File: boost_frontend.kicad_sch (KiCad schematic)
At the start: 25 parts, among them Q1 Q_NMOS, U1 LT8342RV-TRMPBF

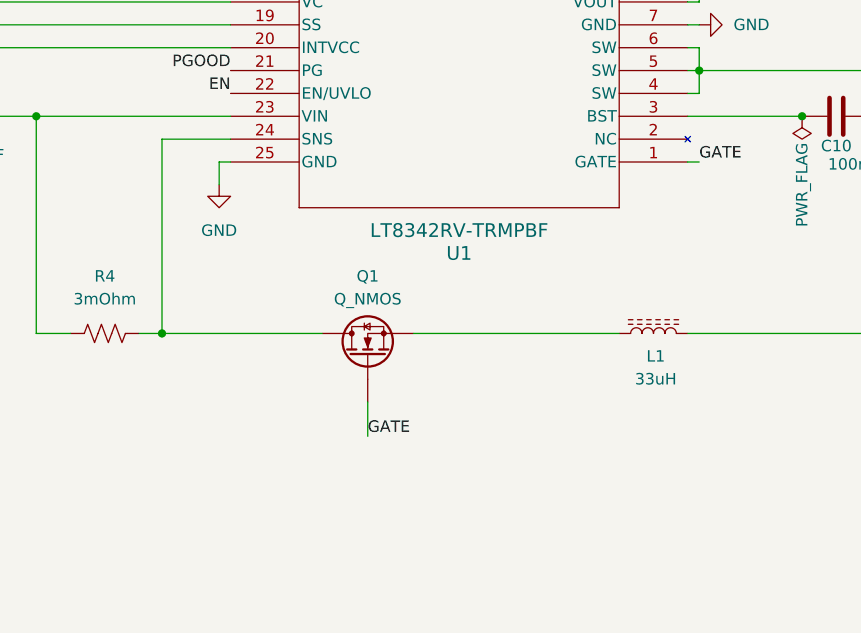
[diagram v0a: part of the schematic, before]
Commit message: routing for power completed
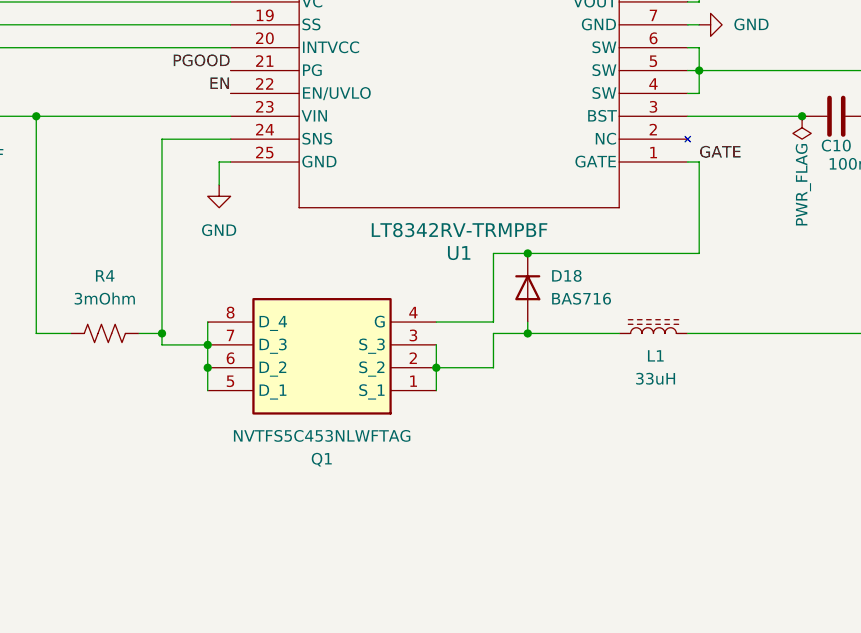
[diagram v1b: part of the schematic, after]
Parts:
- removed Q1: Q_NMOS, Package_DFN_QFN:WDFN-8-1EP_2x2.2mm_P0.5mm_EP0.80x0.54, symbol Device:Q_NMOS
- added D18: BAS716, Diode_SMD:D_SOD-523, symbol Device:D
- added Q1: NVTFS5C453NLWFTAG, NVTFS6H854NTAG, symbol _NVTF:NVTFS5C453NLWFTAG
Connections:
- net GATE: now also D18.1 (K), Q1.4 (G)
- net at R4.2, U1.24 (SNS): now also Q1.5 (D_1), Q1.6 (D_2), Q1.7 (D_3), Q1.8 (D_4)
- net at L1.1: now also D18.2 (A), Q1.1 (S_1), Q1.2 (S_2), Q1.3 (S_3)

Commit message: Working on it
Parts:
- C15, C16, FB2: now not fitted; now left out of the parts list
- renumbered D18 to D1
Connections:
- net Vout is gone; now on net BOOST_OUT: C11.1, C12.1, C13.2, C14.2, FB2.1, U1.10 (VOUT), U1.11 (VOUT), U1.8 (VOUT), U1.9 (VOUT)
- net GND: now also C5.2; no longer C5.1
- net INTVCC: now also R3.2; no longer R3.1
- net at U1.19 (SS): now also C5.1; no longer C5.2
- net at U1.14 (VSET1): now also R3.1; no longer R3.2
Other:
- moved on the sheet: C1, C10, C11, C12, C13, C14, C2, C3, C4, C5, C6, C7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

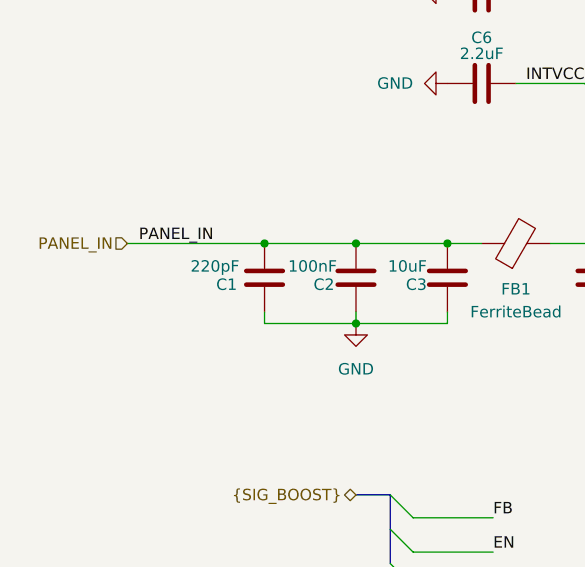
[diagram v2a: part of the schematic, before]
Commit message: Eiditng frontend
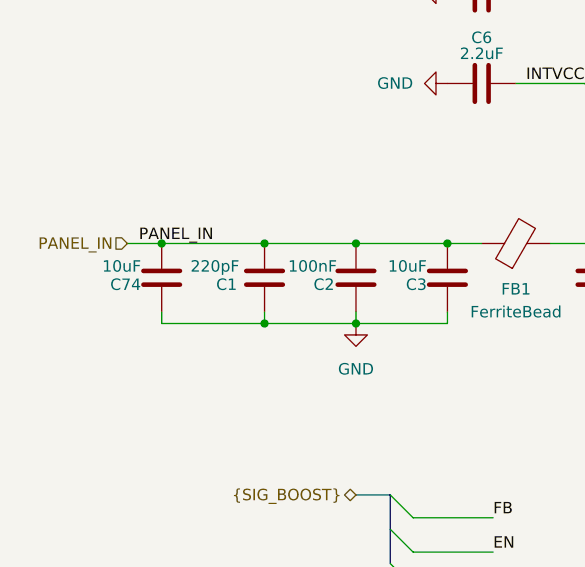
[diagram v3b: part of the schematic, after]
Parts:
- added C74: 10uF, Capacitor_SMD:C_0805_2012Metric, symbol Device:C
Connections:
- net GND: now also C74.1
- net PANEL_IN: now also C74.2
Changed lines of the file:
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@@
+	)
+	(junction
+		(at 31.75 104.14)
+		(diameter 0)
+		(color 0 0 0 0)
 	)
 	(junction
@@
 	(junction
 		(at 154.94 132.08)
+		(diameter 0)
+		(color 0 0 0 0)
+	)
+	(junction
+		(at 43.18 113.03)
 		(diameter 0)
 		(color 0 0 0 0)
@@
 	(wire
 		(pts
+			(xy 31.75 111.76) (xy 31.75 113.03)
+		)
+		(stroke
+			(width 0)
+			(type default)
+		)
+	)
+	(wire
+		(pts
 			(xy 53.34 113.03) (xy 63.5 113.03)
 		)
@@
 	(wire
 		(pts
+			(xy 31.75 113.03) (xy 43.18 113.03)
+		)
+		(stroke
+			(width 0)
+			(type default)
+		)
+	)
+	(wire
+		(pts
 			(xy 132.08 86.36) (xy 124.46 86.36)
 		)
@@
 	(wire
 		(pts
-			(xy 27.94 104.14) (xy 43.18 104.14)
+			(xy 27.94 104.14) (xy 31.75 104.14)
 		)
 		(stroke
@@
 		(pts
 			(xy 100.33 113.03) (xy 100.33 111.76)
+		)
+		(stroke
+			(width 0)
+			(type default)
+		)
+	)
+	(wire
+		(pts
+			(xy 31.75 104.14) (xy 43.18 104.14)
 		)
 		(stroke
@@
 					(unit 1)
 				)
+			)
+		)
+	)
+	(symbol
+		(lib_id "Device:C")
+		(at 31.75 107.95 180)
+		(unit 1)
+		(exclude_from_sim no)
+		(in_bom yes)
+		(on_board yes)
+		(dnp no)
+		(property "Reference" "C74"
+			(at 29.464 108.712 0)
+			(effects
+				(font
+					(size 1.27 1.27)
+				)
+				(justify left)
+			)
+		)
+		(property "Value" "10uF"
+			(at 29.464 106.68 0)
+			(effects
+				(font
+					(size 1.27 1.27)
+				)
+				(justify left)
+			)
+		)
+		(property "Footprint" "Capacitor_SMD:C_0805_2012Metric"
+			(at 30.7848 104.14 0)
+			(effects
+				(font
+					(size 1.27 1.27)
+				)
+				(hide yes)
+			)
+		)
+		(property "Datasheet" "https://search.murata.co.jp/Ceramy/image/img/A01X/G101/ENG/GRM21BR61H106KE43-01A.pdf"
+			(at 31.75 107.95 0)
+			(effects
+				(font
+					(size 1.27 1.27)
+				)
+				(hide yes)
+			)
+		)
+		(property "Description" "CAP CER 10UF 50V X5R 0805"
+			(at 31.75 107.95 0)
+			(effects
+				(font
+					(size 1.27 1.27)
+				)
+				(hide yes)
+			)
+		)
+		(property "Mfr" "Murata Electronics"
+			(at 31.75 107.95 0)
+			(effects
+				(font
+					(size 1.27 1.27)
+				)
+				(hide yes)
+			)
+		)
+		(property "Mfr P/N" "GRM21BR61H106KE43L"
+			(at 31.75 107.95 0)
+			(effects
+				(font
+					(size 1.27 1.27)
+				)
+				(hide yes)
+			)
+		)
+		(property "Supplier_1" "Digikey"
+			(at 31.75 107.95 0)
+			(effects
+				(font
+					(size 1.27 1.27)
+				)
+				(hide yes)
+			)
+		)
+		(property "Supplier_1 P/N" "490-18663-2-ND"
+			(at 31.75 107.95 0)
+			(effects
+				(font
+					(size 1.27 1.27)
+				)
+				(hide yes)
+			)
+		)
+		(property "Supplier_1 Unit Price" "0.28000"
+			(at 31.75 107.95 0)
+			(effects
+				(font
+					(size 1.27 1.27)
+				)
+				(hide yes)
+			)
+		)
+		(property "Supplier_1 Price @ Qty" "1"
+			(at 31.75 107.95 0)
+			(effects
+				(font
+					(size 1.27 1.27)
+				)
+				(hide yes)
+			)
+		)
+		(property "Supplier_2" ""
+			(at 31.75 107.95 0)
+			(effects
+				(font
+					(size 1.27 1.27)
+				)
+				(hide yes)
+			)
+		)
+		(property "Supplier_2 P/N" ""
+			(at 31.75 107.95 0)
+			(effects
+				(font
+					(size 1.27 1.27)
+				)
+				(hide yes)
+			)
+		)
+		(property "Supplier_2 Unit Price" ""
+			(at 31.75 107.95 0)
+			(effects
+				(font
+					(size 1.27 1.27)
+				)
+				(hide yes)
+			)
+		)
+		(property "Supplier_2 Price @ Qty" ""
+			(at 31.75 107.95 0)
+			(effects
+				(font
+					(size 1.27 1.27)
+				)
+				(hide yes)
+			)
+		)
+		(pin "1"
+		)
+		(pin "2"
+		)
+		(instances
+			(project "PowerBoard"
+				(path "/99785679-20de-4827-b4cc-bc3c187068c9/9564929a-642e-4163-88c2-45054b63a5ed/0cef1f69-ed1d-4f02-ab28-a001d17f862e"
+					(reference "C74")
+					(unit 1)
+				)
+				(path "/99785679-20de-4827-b4cc-bc3c187068c9/9564929a-642e-4163-88c2-45054b63a5ed/136865b6-9226-4363-90e9-85327831a678"
+					(reference "C75")
+					(unit 1)
+				)

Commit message: mcu flash v1
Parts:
- L1: value 33uH -> 1.8uH; footprint _PowerBoard:IND_XGL1313_COC-L -> _PowerBoard:XAL6030182MEC; Supplier_1 Digikey -> Mouser; Supplier_1 P/N 2457-SER2918H-333KL-ND -> 994-XAL5030-102MEC; Supplier_1 Unit Price 6.98000 -> 3.50
- R3: value 33.6k -> 100k; Mfr KOA Speer Electronics, Inc. -> Yageo; Mfr P/N RN73R1JTTD3362B25 -> RC0603FR-07100KL; Supplier_1 Digikey -> Mouser; Supplier_1 P/N 2019-RN73R1JTTD3362B25TR-ND -> 603-RC0603FR-07100KL
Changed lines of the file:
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@@
 			)
 		)
-		(property "Value" "33uH"
+		(property "Value" "1.8uH"
 			(at 179.324 137.16 90)
 			(effects
@@
 			)
 		)
-		(property "Footprint" "_PowerBoard:IND_XGL1313_COC-L"
-			(at 179.07 132.08 0)
-			(effects
-				(font
-					(size 1.27 1.27)
-				)
-				(hide yes)
-			)
-		)
-		(property "Datasheet" "https://www.coilcraft.com/getmedia/a2805f49-c9b8-42c0-9939-b2d75eed7288/ser2900.pdf"
-			(at 179.07 132.08 0)
-			(effects
-				(font
-					(size 1.27 1.27)
-				)
-				(hide yes)
-			)
-		)
-		(property "Description" "Inductor with ferrite core"
+		(property "Footprint" "_PowerBoard:XAL6030182MEC"
+			(at 179.07 132.08 0)
+			(effects
+				(font
+					(size 1.27 1.27)
+				)
+				(hide yes)
+			)
+		)
+		(property "Datasheet" "https://www.mouser.com/datasheet/3/995/1/xal50xx.pdf"
+			(at 179.07 132.08 0)
+			(effects
+				(font
+					(size 1.27 1.27)
+				)
+				(hide yes)
+			)
+		)
+		(property "Description" "Power Inductors - SMD 1uH Shld 20% 11.1A 9.4mOhms"
 			(at 179.07 132.08 0)
 			(effects
@@
 			)
 		)
-		(property "Supplier_1" "Digikey"
-			(at 179.07 132.08 0)
-			(effects
-				(font
-					(size 1.27 1.27)
-				)
-				(hide yes)
-			)
-		)
-		(property "Supplier_1 P/N" "2457-SER2918H-333KL-ND"
-			(at 179.07 132.08 0)
-			(effects
-				(font
-					(size 1.27 1.27)
-				)
-				(hide yes)
-			)
-		)
-		(property "Supplier_1 Unit Price" "6.98000"
+		(property "Supplier_1" "Mouser"
+			(at 179.07 132.08 0)
+			(effects
+				(font
+					(size 1.27 1.27)
+				)
+				(hide yes)
+			)
+		)
+		(property "Supplier_1 P/N" "994-XAL5030-102MEC"
+			(at 179.07 132.08 0)
+			(effects
+				(font
+					(size 1.27 1.27)
+				)
+				(hide yes)
+			)
+		)
+		(property "Supplier_1 Unit Price" "3.50"
 			(at 179.07 132.08 0)
 			(effects
@@
 			)
 		)
-		(property "Value" "33.6k"
+		(property "Value" "100k"
 			(at 96.52 53.34 90)
 			(effects
@@
 			)
 		)
-		(property "Datasheet" "https://www.koaspeer.com/pdfs/RN73R.pdf"
+		(property "Datasheet" "https://www.mouser.com/catalog/specsheets/YAGEO_PYu_RC_Group_51_RoHS_L_12.pdf"
 			(at 96.52 55.88 0)
 			(effects
@@
 			)
 		)
-		(property "Mfr" "KOA Speer Electronics, Inc."
+		(property "Mfr" "Yageo"
 			(at 96.52 55.88 0)
 			(effects
@@
 			)
 		)
-		(property "Mfr P/N" "RN73R1JTTD3362B25"
+		(property "Mfr P/N" "RC0603FR-07100KL "
 			(at 96.52 55.88 0)
 			(effects
@@
 			)
 		)
-		(property "Supplier_1" "Digikey"
+		(property "Supplier_1" "Mouser"
 			(at 96.52 55.88 0)
 			(effects
@@
 			)
 		)
-		(property "Supplier_1 P/N" "2019-RN73R1JTTD3362B25TR-ND"
+		(property "Supplier_1 P/N" "603-RC0603FR-07100KL"
 			(at 96.52 55.88 0)
 			(effects

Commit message: Working on schematic and layout
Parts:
- removed U1: LT8342RV-TRMPBF, _PowerBoard:05-08-7040_ADI, symbol _LT8342:LT8342RV-TRMPBF
- added U6: LT8342RV-TRMPBF, _PowerBoard:05-08-7040_ADI, symbol _LT8342:LT8342RV-TRMPBF
- Q1: footprint NVTFS6H854NTAG -> _PowerBoard:NVTFS6H854NTAG
- renumbered C74 to C1, C9 to C10, C10 to C11, C11 to C12, C12 to C13, C13 to C14, C14 to C15, C15 to C16, C16 to C17, C1 to C2, C2 to C3, C3 to C4, C4 to C5, C5 to C6, C6 to C7, C7 to C8, C8 to C9
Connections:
- net BOOST_OUT: now also U6.10 (VOUT), U6.11 (VOUT), U6.8 (VOUT), U6.9 (VOUT)
- net EN: now also U6.22 (EN/UVLO)
- net FB: now also U6.13 (VSET2/FB)
- net GATE: now also U6.1 (GATE)
- net GND: now also U6.12 (GND), U6.15 (PREBOOST), U6.16 (SYNC/MODE), U6.25 (GND), U6.7 (GND)
- net INTVCC: now also U6.20 (INTVCC)
- net PGOOD: now also U6.21 (PG)
- net at Q1.5 (D_1), Q1.6 (D_2), Q1.7 (D_3)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: now also U6.24 (SNS)
- net at R1.2: now also U6.17 (RT)
- net at C10.2, C8.2, C9.1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: now also U6.23 (VIN)
- net at R2.2: now also U6.18 (VC)
- net at C11.1, L1.2: now also U6.4 (SW), U6.5 (SW), U6.6 (SW)
- net at C6.1: now also U6.19 (SS)
- net at C11.2: now also U6.3 (BST)
- net at R3.1: now also U6.14 (VSET1)

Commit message: Pushing
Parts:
- added R43: R, symbol Device:R
- L1: Supplier_2 (none) -> JLCPCB; Supplier_2 P/N (none) -> C19191693; Supplier_2 Price @ Qty (none) -> 1; Supplier_2 Unit Price (none) -> 1.5264
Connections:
- net PGOOD: now also R43.2
- new net +3V3: R43.1
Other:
- note added: "PGOOD pull-up"
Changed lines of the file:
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@@
 		)
 	)
+	(text "PGOOD pull-up"
+		(exclude_from_sim no)
+		(at 105.41 137.922 0)
+		(effects
+			(font
+				(size 1.27 1.27)
+			)
+		)
+	)
 	(text "Compensation network"
 		(exclude_from_sim no)
@@
 	(wire
 		(pts
+			(xy 90.17 143.51) (xy 90.17 140.97)
+		)
+		(stroke
+			(width 0)
+			(type default)
+		)
+	)
+	(wire
+		(pts
 			(xy 182.88 96.52) (xy 184.15 96.52)
 		)
@@
 	(wire
 		(pts
-			(xy 59.69 142.24) (xy 68.58 142.24)
+			(xy 59.69 142.24) (xy 72.39 142.24)
 		)
 		(stroke
@@
 	(wire
 		(pts
-			(xy 59.69 138.43) (xy 68.58 138.43)
+			(xy 59.69 138.43) (xy 72.39 138.43)
 		)
 		(stroke
@@
 	(wire
 		(pts
-			(xy 59.69 134.62) (xy 68.58 134.62)
+			(xy 59.69 134.62) (xy 72.39 134.62)
 		)
 		(stroke
@@
 	)
 	(label "EN"
-		(at 68.58 138.43 0)
+		(at 72.39 138.43 0)
 		(effects
 			(font
@@
 		)
 	)
+	(label "PGOOD"
+		(at 90.17 143.51 0)
+		(effects
+			(font
+				(size 1.27 1.27)
+			)
+			(justify left bottom)
+		)
+	)
 	(label "FB"
-		(at 68.58 134.62 0)
+		(at 72.39 134.62 0)
 		(effects
 			(font
@@
 	)
 	(label "PGOOD"
-		(at 68.58 142.24 0)
+		(at 72.39 142.24 0)
 		(effects
 			(font
@@
 	)
 	(symbol
+		(lib_id "power:+3V3")
+		(at 90.17 133.35 0)
+		(unit 1)
+		(exclude_from_sim no)
+		(in_bom yes)
+		(on_board yes)
+		(dnp no)
+		(fields_autoplaced yes)
+		(property "Reference" "#PWR0165"
+			(at 90.17 137.16 0)
+			(effects
+				(font
+					(size 1.27 1.27)
+				)
+				(hide yes)
+			)
+		)
+		(property "Value" "+3V3"
+			(at 90.17 128.27 0)
+			(effects
+				(font
+					(size 1.27 1.27)
+				)
+			)
+		)
+		(property "Footprint" ""
+			(at 90.17 133.35 0)
+			(effects
+				(font
+					(size 1.27 1.27)
+				)
+				(hide yes)
+			)
+		)
+		(property "Datasheet" ""
+			(at 90.17 133.35 0)
+			(effects
+				(font
+					(size 1.27 1.27)
+				)
+				(hide yes)
+			)
+		)
+		(property "Description" "Power symbol creates a global label with name \"+3V3\""
+			(at 90.17 133.35 0)
+			(effects
+				(font
+					(size 1.27 1.27)
+				)
+				(hide yes)
+			)
+		)
+		(pin "1"
+		)
+		(instances
+			(project ""
+				(path "/99785679-20de-4827-b4cc-bc3c187068c9/9564929a-642e-4163-88c2-45054b63a5ed/0cef1f69-ed1d-4f02-ab28-a001d17f862e"
+					(reference "#PWR0165")
+					(unit 1)
+				)
+				(path "/99785679-20de-4827-b4cc-bc3c187068c9/9564929a-642e-4163-88c2-45054b63a5ed/136865b6-9226-4363-90e9-85327831a678"
+					(reference "#PWR0170")
+					(unit 1)
+				)
+			)
+		)
+	)
+	(symbol
 		(lib_id "Device:C_Polarized_US")
 		(at 90.17 107.95 0)
@@
 	)
 	(symbol
+		(lib_id "Device:R")
+		(at 90.17 137.16 0)
+		(unit 1)
+		(exclude_from_sim no)
+		(in_bom yes)
+		(on_board yes)
+		(dnp no)
+		(fields_autoplaced yes)
+		(property "Reference" "R43"
+			(at 92.71 135.8899 0)
+			(effects
+				(font
+					(size 1.27 1.27)
+				)
+				(justify left)
+			)
+		)
+		(property "Value" "R"
+			(at 92.71 138.4299 0)
+			(effects
+				(font
+					(size 1.27 1.27)
+				)
+				(justify left)
+			)
+		)
+		(property "Footprint" ""
+			(at 88.392 137.16 90)
+			(effects
+				(font
+					(size 1.27 1.27)
+				)
+				(hide yes)
+			)
+		)
+		(property "Datasheet" "~"
+			(at 90.17 137.16 0)
+			(effects
+				(font
+					(size 1.27 1.27)
+				)
+				(hide yes)
+			)
+		)
+		(property "Description" "Resistor"
+			(at 90.17 137.16 0)
+			(effects
+				(font
+					(size 1.27 1.27)
+				)
+				(hide yes)
+			)
+		)
+		(pin "2"
+		)
+		(pin "1"
+		)
+		(instances
+			(project ""
+				(path "/99785679-20de-4827-b4cc-bc3c187068c9/9564929a-642e-4163-88c2-45054b63a5ed/0cef1f69-ed1d-4f02-ab28-a001d17f862e"
+					(reference "R43")
+					(unit 1)
+				)
+				(path "/99785679-20de-4827-b4cc-bc3c187068c9/9564929a-642e-4163-88c2-45054b63a5ed/136865b6-9226-4363-90e9-85327831a678"
+					(reference "R44")
+					(unit 1)
+				)
+			)
+		)
+	)
+	(symbol
 		(lib_id "Device:FerriteBead")
 		(at 243.84 86.36 90)
@@
 			)
 		)
-		(property "Supplier_2" ""
+		(property "Supplier_2" "JLCPCB"
 			(at 179.07 132.08 0)
 			(effects
@@
 			)
 		)
-		(property "Supplier_2 P/N" ""
+		(property "Supplier_2 P/N" "C19191693"
 			(at 179.07 132.08 0)
 			(effects
@@
 			)
 		)
-		(property "Supplier_2 Unit Price" ""
+		(property "Supplier_2 Unit Price" "1.5264"
 			(at 179.07 132.08 0)
 			(effects
@@
 			)
 		)
-		(property "Supplier_2 Price @ Qty" ""
+		(property "Supplier_2 Price @ Qty" "1"
 			(at 179.07 132.08 0)
 			(effects

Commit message: BOM in folder
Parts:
- removed R43: R, symbol Device:R
- added R39: 10k, Resistor_SMD:R_0603_1608Metric, symbol Device:R
- C1, C10, C14, C15, C4: Supplier_1 Digikey -> LCSC; Supplier_1 P/N 490-18663-2-ND -> C440198; Supplier_1 Unit Price 0.28000 -> (none)
- C11, C12, C13, C16, C3, C6, C8: JLCPCB Status (none) -> JLC in-stock package match; Mfr P/N 06035C104K4T2A -> CC0603KRX7R9BB104; Supplier_1 Digikey -> LCSC; Supplier_1 P/N 478-KAM15AR71H104KTTR-ND -> C14663; Supplier_1 Unit Price 0.10000 -> (none)
- C17, C2: JLCPCB Status (none) -> JLC in-stock package match; Mfr P/N GCM1885C2A221FA16J -> CL10B221KB8NNNC; Supplier_1 Digikey -> LCSC; Supplier_1 P/N 490-GCM1885C2A221FA16JTR-ND -> C1603; Supplier_1 Unit Price 0.14000 -> (none)
- C5: JLCPCB Status (none) -> JLC in-stock package match; Mfr P/N GCM1885C1H332FA16D -> CL10B333KB8NNNC; Supplier_1 Digikey -> LCSC; Supplier_1 P/N 490-GCM1885C1H332FA16DTR-ND -> C21117; Supplier_1 Unit Price 0.17000 -> (none)
- C7: Supplier_1 Digikey -> LCSC; Supplier_1 P/N 490-12332-2-ND -> C668370; Supplier_1 Unit Price 0.27000 -> (none)
- C9: Supplier_1 Digikey -> LCSC; Supplier_1 P/N 493-16369-2-ND -> C507620; Supplier_1 Unit Price 1.06000 -> (none)
- D1: JLCPCB Status (none) -> JLC in-stock package match; Mfr P/N (none) -> BAS716; Supplier_1 (none) -> LCSC; Supplier_1 P/N (none) -> C5292819
- FB1: Supplier_1 Digikey -> LCSC; Supplier_1 P/N 240-HR2220V701R-10TR-ND -> C2614378; Supplier_1 Unit Price 2.57000 -> (none)
- FB2: Supplier_1 Digikey -> LCSC; Supplier_1 P/N 732-13782-2-ND -> C5149220; Supplier_1 Unit Price 0.30000 -> (none)
- L1: Supplier_1 Mouser -> LCSC; Supplier_1 P/N 994-XAL5030-102MEC -> C3911813; Supplier_1 Unit Price 3.50 -> (none)
- Q1: Supplier_1 (none) -> LCSC; Supplier_1 P/N (none) -> C145551
- R1: Supplier_1 Digikey -> LCSC; Supplier_1 P/N 2019-RN73R1JTTD3362B25TR-ND -> C22800; Supplier_1 Unit Price 0.04314 -> (none)
- R2: Supplier_1 Digikey -> LCSC; Supplier_1 P/N 2019-RN73H1JTTD6042B25TR-ND -> C23228; Supplier_1 Unit Price 0.10000 -> (none)
- R3: Supplier_1 Mouser -> LCSC; Supplier_1 P/N 603-RC0603FR-07100KL -> C14675; Supplier_1 Unit Price 0.04314 -> (none)
- R4: Supplier_1 (none) -> LCSC; Supplier_1 P/N (none) -> C728307
- U6: Supplier_1 Digikey -> LCSC; Supplier_1 P/N 505-LT8342RV#TRPBFTR-ND -> C41557266; Supplier_1 Unit Price 11.03000 -> (none)
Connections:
- net +3V3: now also R39.1
- net PGOOD: now also R39.2
